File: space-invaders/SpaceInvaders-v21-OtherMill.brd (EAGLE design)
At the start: 91.4 x 91.4 mm, 27 parts, among them J2-J4 TM4C123GXL, J3-J1 TM4C123GXL, J5 NOKIA_5110, J6 NOKIA_5110, J7 9V, U1 LM7805CT

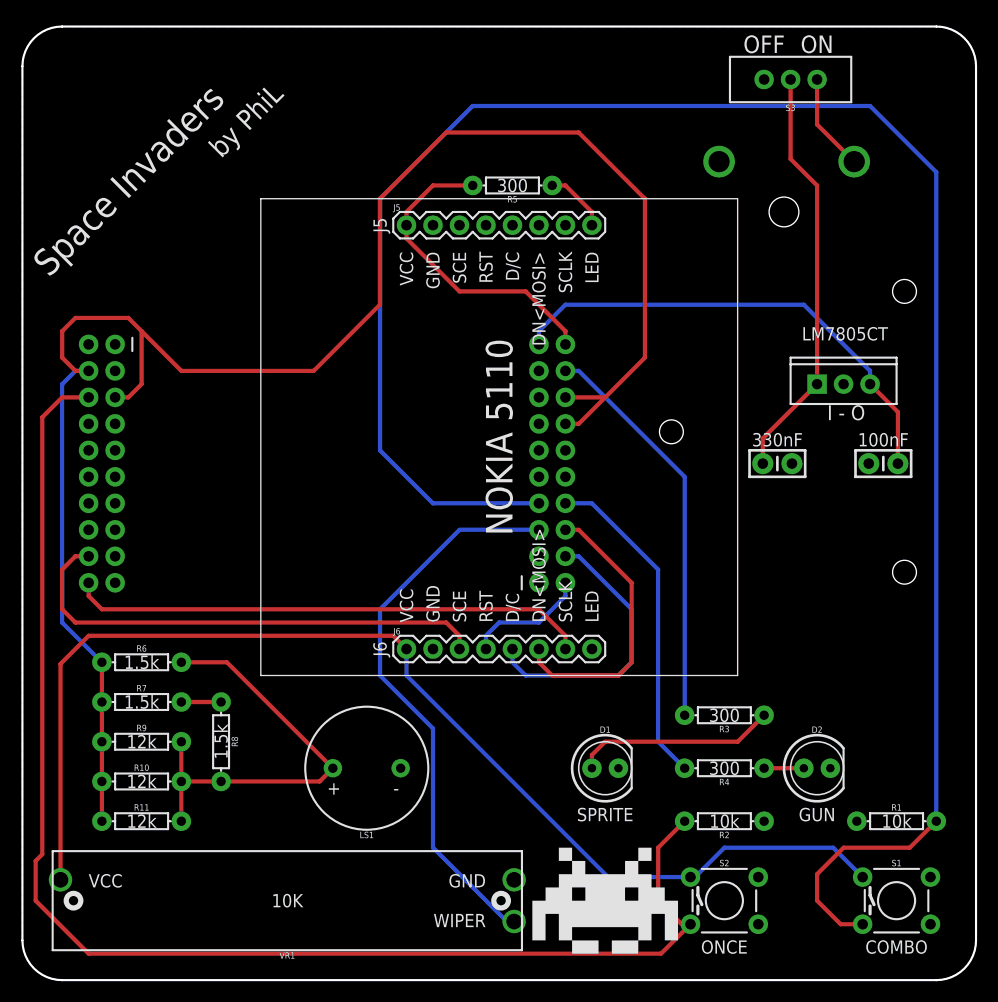
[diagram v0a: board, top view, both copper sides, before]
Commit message: Edit trivial parts for Space Invaders
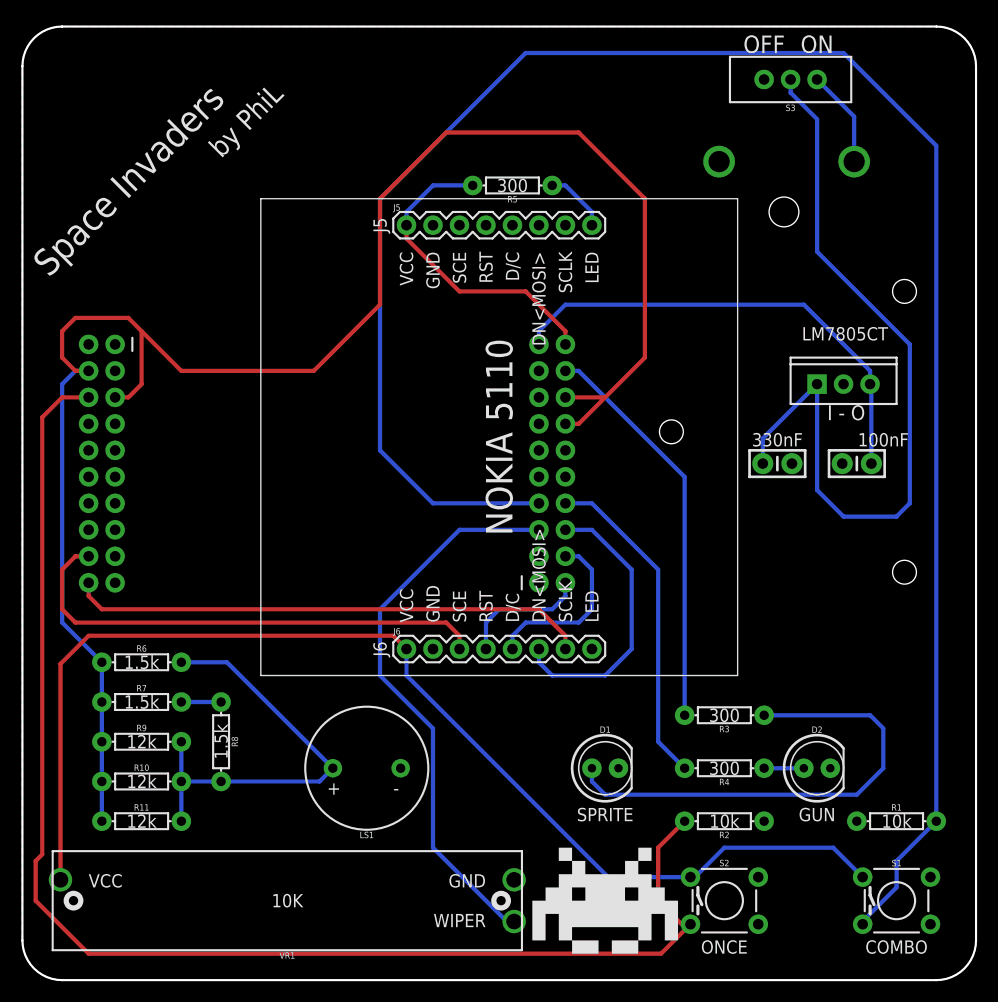
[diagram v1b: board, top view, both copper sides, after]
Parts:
- moved C1 2.54 mm to (80.0, 49.5)
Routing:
- net VIN: track 40.0 -> 75.8 mm
- net LLED: track 19.4 -> 46.6 mm
- net PA6: track 27.3 -> 16.8 mm
- net PE1: track 184.7 -> 181.9 mm
- net VBUS: track 46.7 -> 45.6 mm
- net PA7: track 11.7 -> 12.5 mm
- added copper zone on layer 1, net GND
